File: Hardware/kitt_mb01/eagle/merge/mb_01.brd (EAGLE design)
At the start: 160 x 100 mm, 125 parts, among them CON1 ARDUINO_UNO, IC1.01 RT8293A, IC2.00 BQ24266RGET, IC3.01 LSM9DS1, P2 S2B-PH-K-S(LF)(SN), U0.1 SI1922EDH, U6.01 TPS61032RSARPSDO-G16, U7.01 SI1922EDH, U7.2 SI1922EDH, X1 CON_HEADER_1X02, X2 CON_HEADER_1X02, X3 CON_HEADER_1X02, X4 CON_HEADER_1X02, X7.05 MOTOR

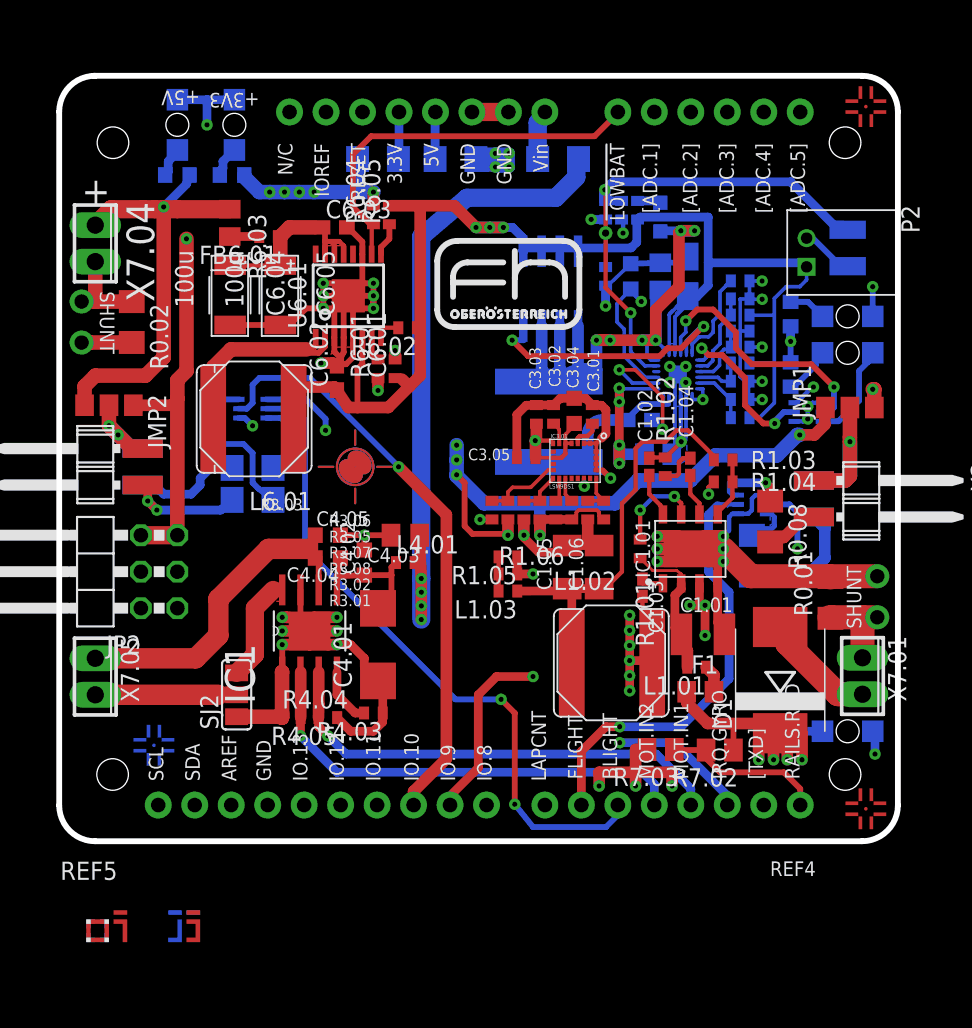
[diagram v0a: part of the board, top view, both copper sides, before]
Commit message: board merge snapshot : semivalid edition -> ran through first DRC for Würth standard manufacture -> corrected 262 errors
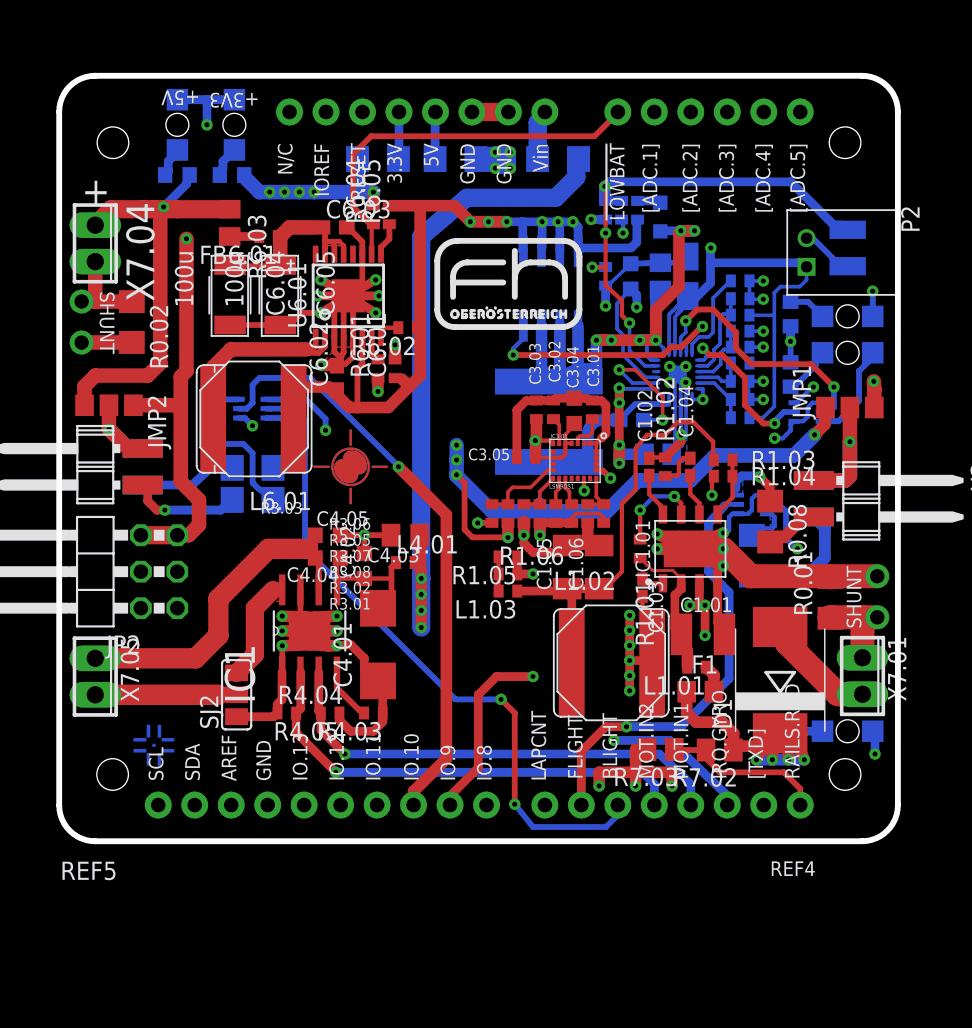
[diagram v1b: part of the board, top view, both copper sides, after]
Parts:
- removed REF1: REF.LAYERS, kitt.refs:REF_LAYERS
- removed U$7, U$9: (no value), marks:PASSER-CIRCLE
- moved C2.03 0.56 mm to (86.6, 49.9)
- moved R4.04 0.45 mm to (62.5, 29.5)
- moved R1.04 0.40 mm to (92.9, 46.0)
- moved R4.05 0.35 mm to (65.6, 29.5)
- moved C3.01 0.32 mm to (83.8, 50.6)
- moved C3.02 0.32 mm to (81.1, 50.6)
- moved C3.03 0.32 mm to (79.9, 50.6)
- moved U$5 0.32 mm to (67.0, 46.7)
- moved C4.02 0.24 mm to (67.9, 39.8)
- moved R3.01 0.24 mm to (84.6, 43.4)
- moved R3.02 0.24 mm to (83.5, 43.4)
- moved R3.03 0.24 mm to (77.9, 43.4)
- moved R3.04 0.24 mm to (76.8, 43.4)
- moved R3.05 0.24 mm to (80.2, 43.4)
- moved R3.06 0.24 mm to (79.1, 43.4)
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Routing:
- net +4.1V: track 99.8 -> 114.5 mm, vias 3 -> 7
- net N$49: track 13.7 -> 0.00 mm
- net GND: track 246.0 -> 239.2 mm, vias 48 -> 47
- net +3V3: track 151.7 -> 155.5 mm
- net +12V: track 104.9 -> 108.0 mm
- net +5V: track 149.0 -> 151.6 mm
- net MOT.IN2: track 33.8 -> 32.3 mm
- net N$87: track 29.3 -> 30.6 mm
- net N$7: track 5.54 -> 4.31 mm
- net N$46: track 9.33 -> 8.43 mm, vias 2 -> 1
- net V+: track 15.4 -> 16.2 mm
- net N$52: track 7.73 -> 6.90 mm
- net MOT.IN1: track 33.6 -> 32.9 mm
- net N$15: track 37.0 -> 36.9 mm, vias 3 -> 4
- net N$48: track 7.44 -> 7.48 mm, vias 2 -> 1
- added copper zone on layer 16, net N$7

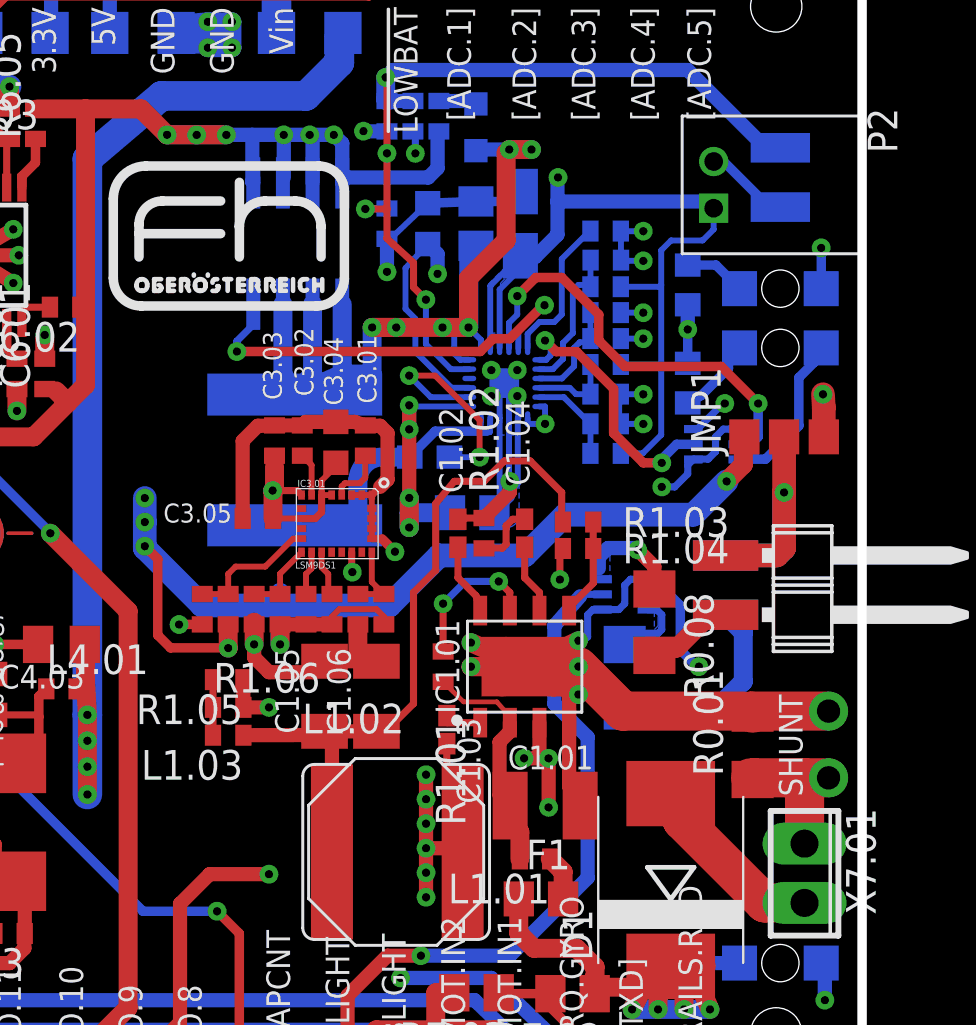
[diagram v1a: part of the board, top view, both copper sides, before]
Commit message: board merge snapshot : 100 down, more to go version -> approved of SMT pad overlaps (for IC1.01 and IC3.01) -> some wires may need reroute
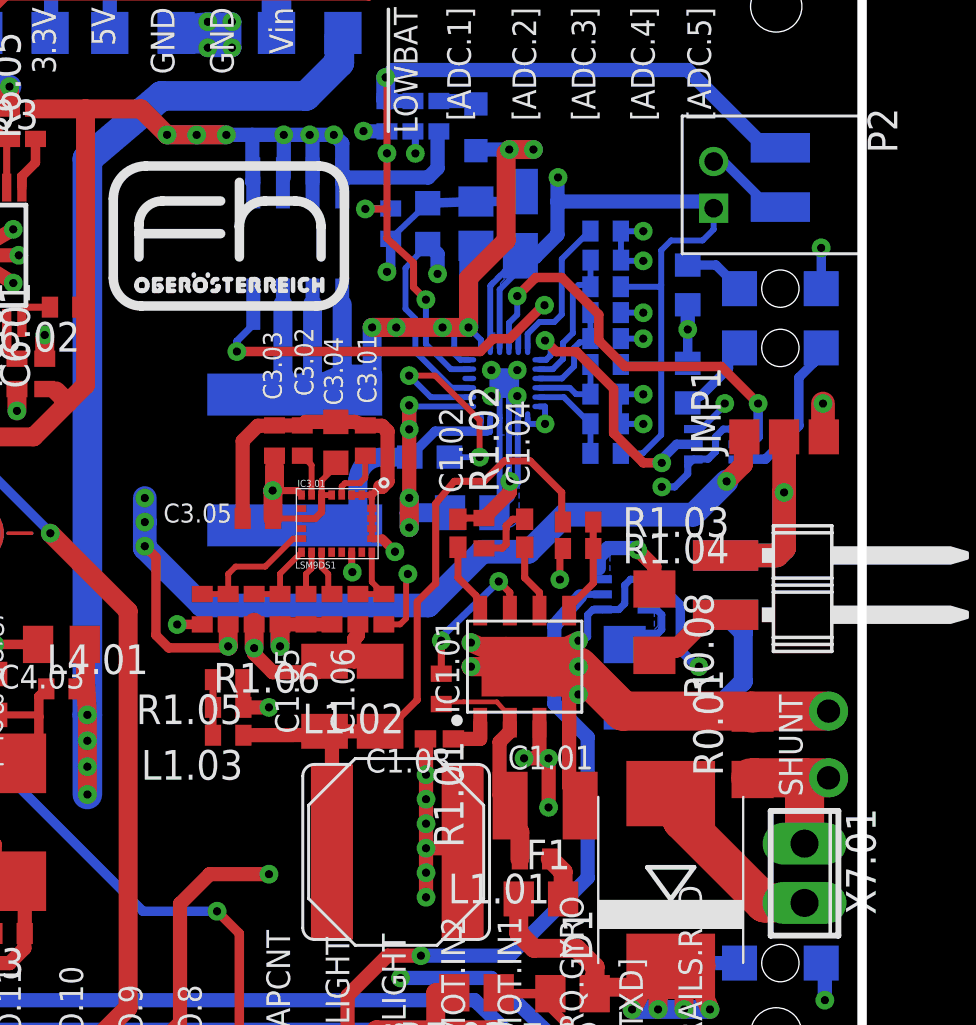
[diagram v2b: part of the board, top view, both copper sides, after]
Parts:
- moved R1.01 0.96 mm to (87.1, 40.0)
- moved C1.03 0.51 mm to (87.0, 37.9), turned to 180 degrees
- moved C1.06 0.16 mm to (84.5, 39.7)
- moved R2.05 0.16 mm to (84.9, 59.9)
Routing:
- net +3V3: track 155.5 -> 161.2 mm, vias 14 -> 15
- net N$88: track 16.2 -> 13.2 mm
- net +5V: track 151.6 -> 153.5 mm
- net CAR.SPEED: track 29.5 -> 30.3 mm
- net GND: track 239.2 -> 238.7 mm

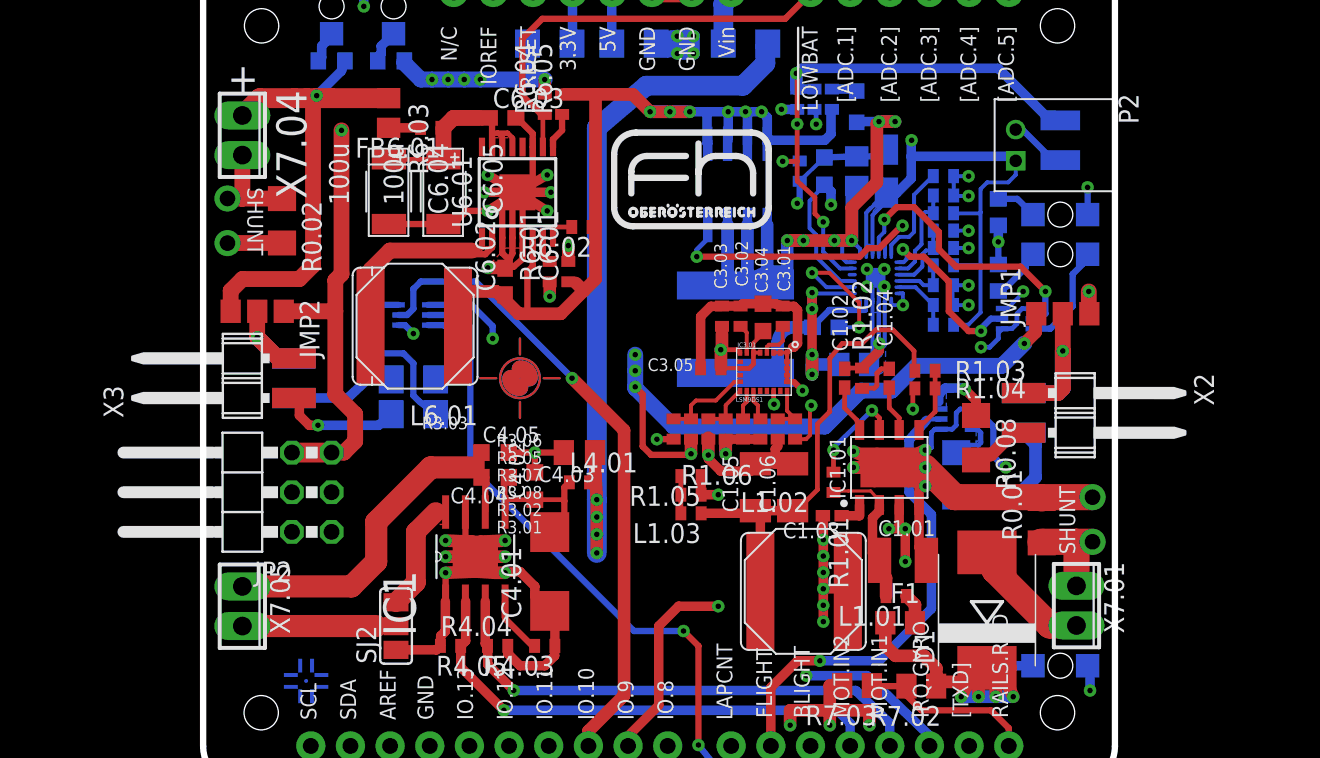
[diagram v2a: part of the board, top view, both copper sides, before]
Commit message: exported bill of materials, soon to be annotated with part# from vendors
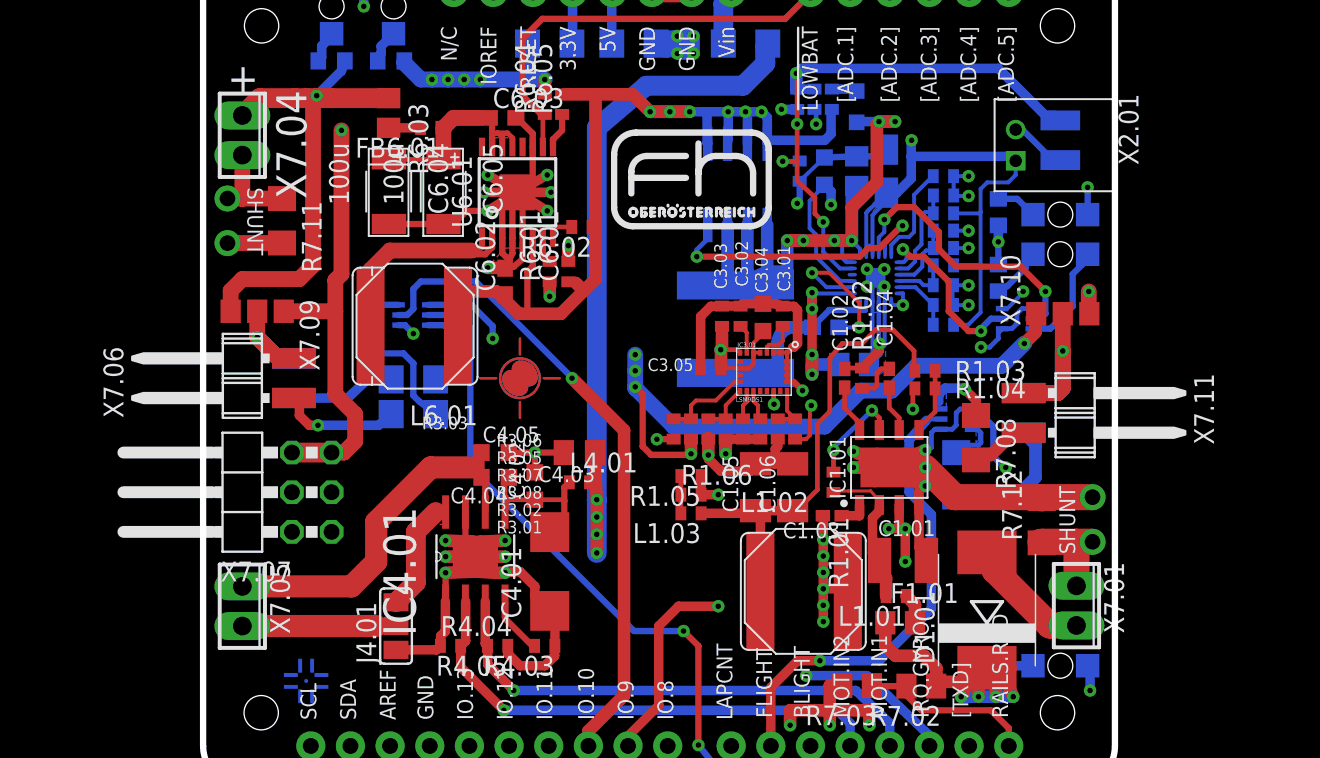
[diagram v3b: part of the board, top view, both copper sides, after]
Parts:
- removed X1, X2, X3, X4: CON_HEADER_1X02, kitt.con:M1X2_MALE_RIGHT_ANGLED_SMD
- added X7.03, X7.06, X7.08, X7.11: CON_HEADER_1X02, kitt.con:M1X2_MALE_RIGHT_ANGLED_SMD
- renumbered CON1 to X7.02, D1 to D1.01, F1 to F1.01, IC1 to IC4.01, JMP1 to X7.10, JMP2 to X7.09, JP2 to X7.07, P2 to X2.01, Q1 to Q2.01, R0.01 to R7.12, R0.02 to R7.11, R0.03 to R7.04, R0.04 to R7.09, R0.05 to R7.05, R0.06 to R7.06, R0.07 to R7.07, R0.08 to R7.08, R0.09 to R7.10, SJ2 to J4.01
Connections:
- net N$42: now also X7.08.1; no longer X1.1
- net N$45: now also X7.08.2, X7.11.1; no longer X1.2, X2.1
- net N$46: now also X7.06.1; no longer X3.1
- net N$48: now also X7.03.1, X7.06.2; no longer X3.2, X4.1
- net N$50: now also X7.11.2; no longer X2.2
- net N$52: now also X7.03.2; no longer X4.2

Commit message: updated bill of materials, changed some footprints
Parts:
- added R1: (no value), rcl:R0805
- added R2: (no value), rcl:R0402
- F1.01: device rcl:R0805 -> rcl:R1210
- moved L1.02 0.79 mm to (84.1, 33.0)
- moved F1.01 0.48 mm to (91.3, 30.5)
- moved C1.01 0.45 mm to (91.2, 34.7)
- moved C1.03 0.32 mm to (87.3, 37.9)
- moved L1.01 0.08 mm to (91.1, 32.6)
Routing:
- net N$88: track 13.2 -> 16.3 mm, vias 9 -> 11
- net GND: track 238.7 -> 240.1 mm
- net N$80: track 1.94 -> 2.49 mm
- net N$81: track 10.1 -> 10.6 mm
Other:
- board text added: "CHANGE LED RES TO 0805"

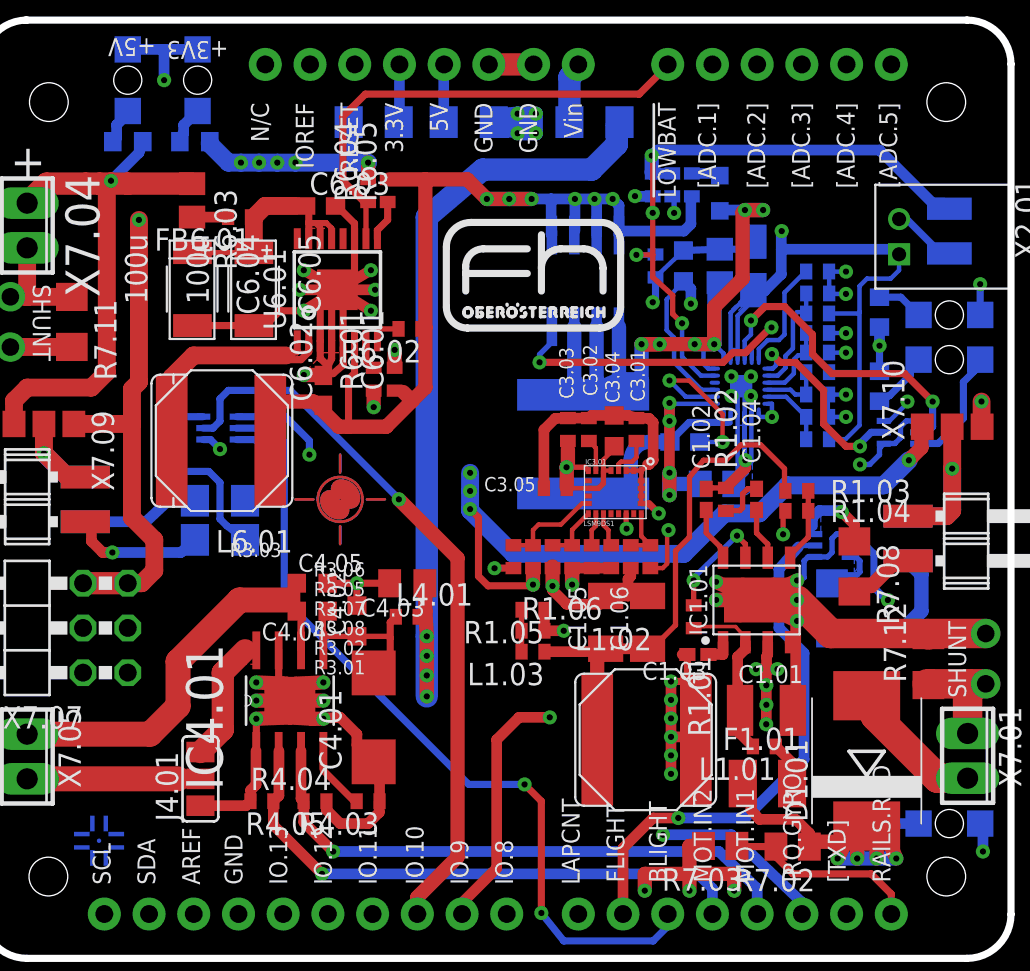
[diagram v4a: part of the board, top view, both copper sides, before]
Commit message: swapped footprint of LED resistors from 1206 to 0402
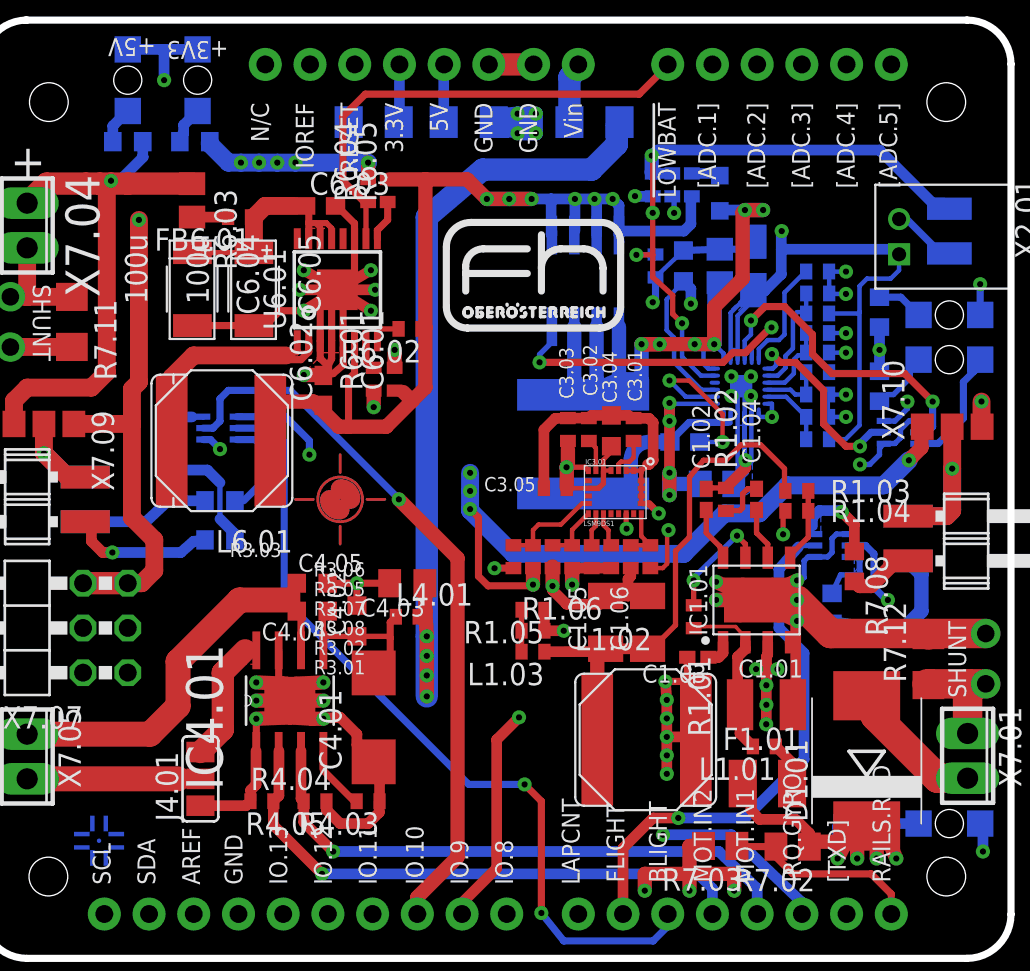
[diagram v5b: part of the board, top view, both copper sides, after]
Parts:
- R7.04, R7.08, R7.09, R7.10: device rcl:R1206 -> rcl:R0603
- moved R7,05 0.79 mm to (96.4, 28.3)
- moved C1.01 0.32 mm to (91.2, 35.0)
- moved C1.03 0.16 mm to (87.3, 37.7)
- moved C3.01 0.16 mm to (83.7, 50.6)
- moved C3.04 0.16 mm to (82.4, 50.6)
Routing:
- net +12V: track 107.9 -> 104.7 mm
- net !IRQ_GYRO: track 34.9 -> 37.4 mm
- net CAR.GATECTLR: track 41.0 -> 40.2 mm
- net N$44: track 1.84 -> 2.64 mm
- net +3V3: track 161.2 -> 160.5 mm
- net N$7: track 4.31 -> 4.88 mm
- net N$52: track 6.90 -> 7.47 mm
- net N$46: track 8.43 -> 8.98 mm
- net +5V: track 153.5 -> 154.0 mm
